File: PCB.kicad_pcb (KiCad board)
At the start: 2 copper layers, 60 x 60 mm, 50 parts, among them J1 USB_C_Receptacle_USB2.0_16P, J2 Conn_01x04_Pin, J3 Conn_01x04_Pin, J4 Conn_01x04_Pin, J5 Conn_01x02_Pin, J6 Conn_01x02_Pin, J7 Conn_01x02_Pin, SW1 SW_Push, SW2 SW_Push, U1 TMC2209_SILENTSTEPSTICK, U2 TMC2209_SILENTSTEPSTICK, U3 D3V3XA4B10LP, U4 AMS1117-3.3 (UMW), U5 TMC2209_SILENTSTEPSTICK, U6 ESP32-S3-WROOM-1

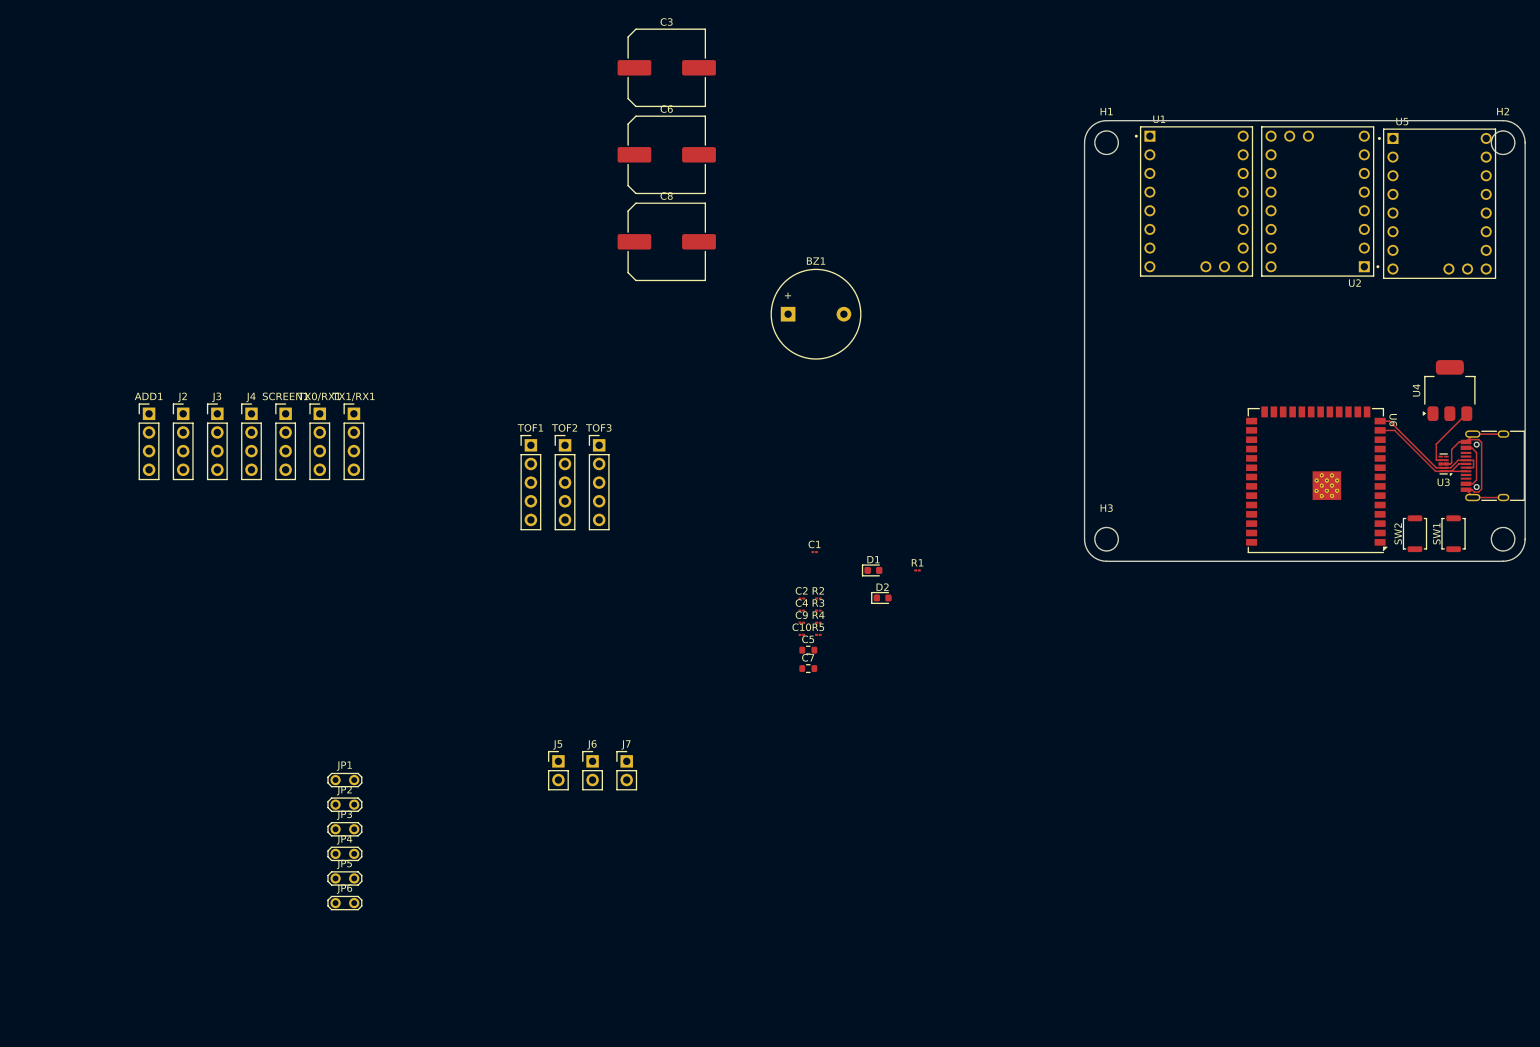
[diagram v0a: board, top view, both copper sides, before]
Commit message: Correction bug schématic
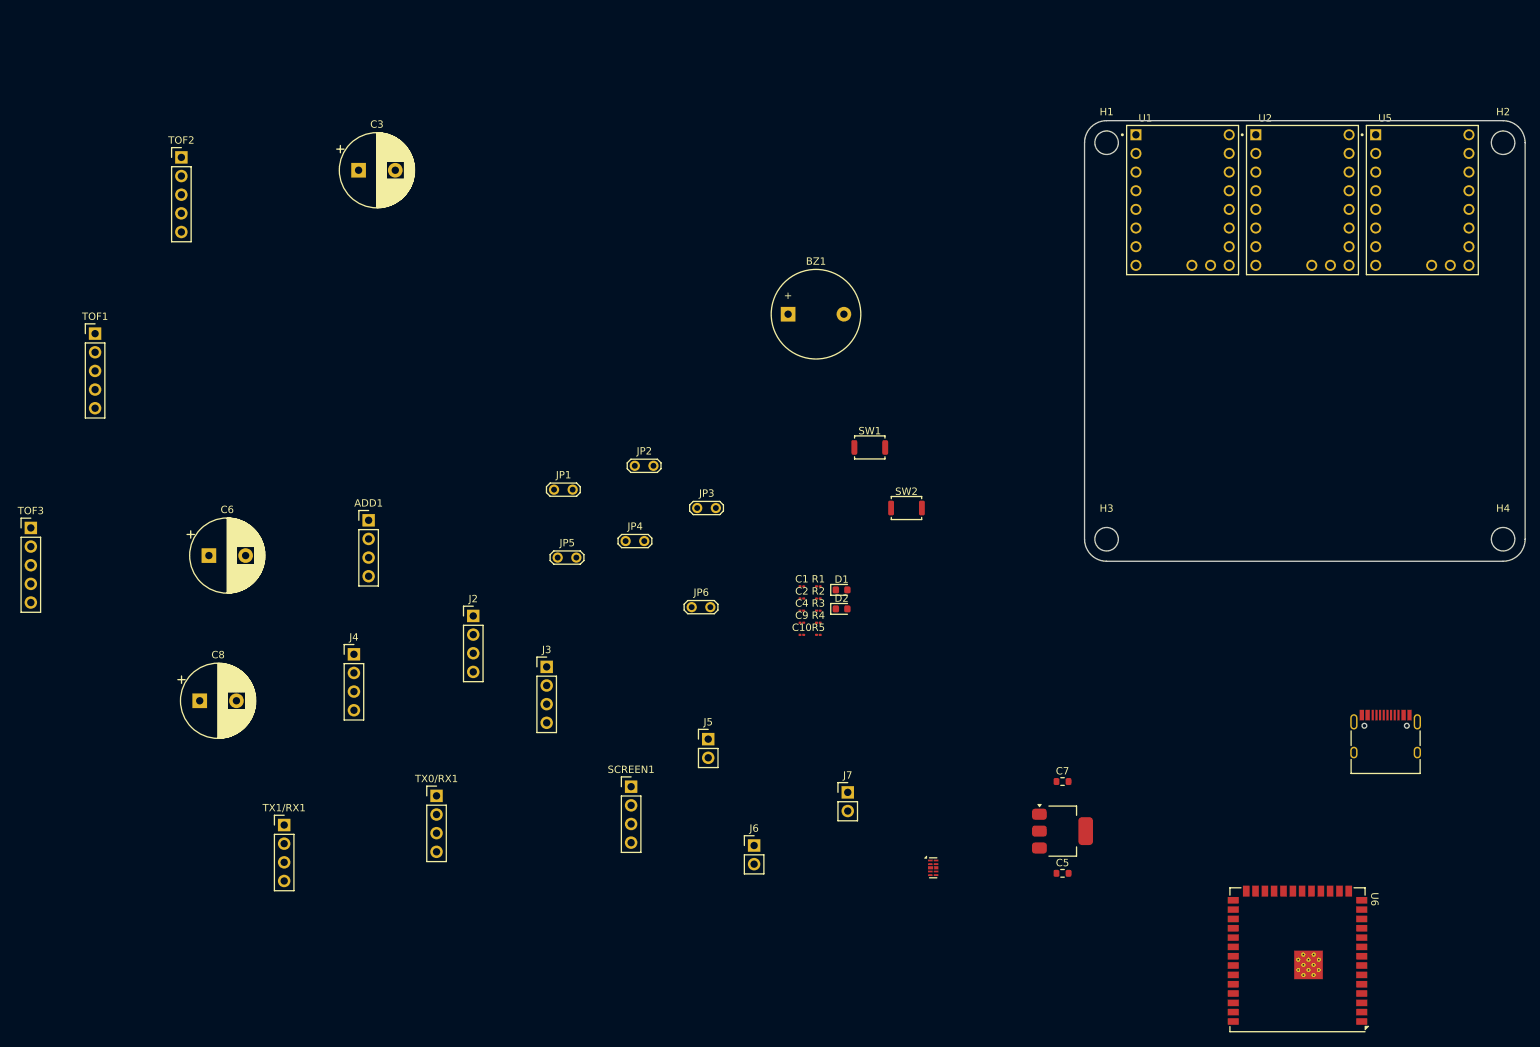
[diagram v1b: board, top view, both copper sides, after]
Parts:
- C3, C6, C8: footprint Capacitor_SMD:C_Elec_10x10.2 -> Capacitor_THT:CP_Radial_D10.0mm_P5.00mm
- moved C8 89.2 mm to (89.5, 126.0)
- moved U3 88.6 mm to (189.4, 148.8), turned to 0 degrees
- moved C6 82.9 mm to (90.8, 106.2)
- moved SW1 80.4 mm to (180.8, 91.5), turned to 0 degrees
- moved U4 79.9 mm to (207.0, 143.8), turned to 0 degrees
- moved TOF3 78.2 mm to (66.5, 102.5)
- moved SW2 69.3 mm to (185.8, 99.8), turned to 0 degrees
- moved SCREEN1 69.2 mm to (148.2, 137.7)
- moved JP3 65.9 mm to (157.2, 99.8)
- moved TOF2 65.3 mm to (87.0, 52.0)
- moved U6 65.3 mm to (239.0, 161.3)
- moved JP6 63.1 mm to (156.5, 113.2)
- moved JP2 61.6 mm to (148.8, 94.0)
- moved TOF1 61.3 mm to (75.2, 76.0)
- moved JP4 58.1 mm to (147.5, 104.2)
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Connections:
- ADD1 pad 4: 3V3 -> GND
- BZ1 pad 2: 3V3 -> GND
- C1 pad 2: 3V3 -> GND
- C10 pad 2: 3V3 -> GND
- C2 pad 2: 3V3 -> GND
- C3 pad 2: 3V3 -> GND
- C4 pad 2: 3V3 -> GND
- C5 pad 2: 3V3 -> GND
- C6 pad 2: 3V3 -> GND
- C7 pad 2: 3V3 -> GND
- C8 pad 2: 3V3 -> GND
- C9 pad 2: 3V3 -> GND
- J1 pad A1: 3V3 -> GND
- J1 pad A12: 3V3 -> GND
- J1 pad B1: 3V3 -> GND
- J1 pad B12: 3V3 -> GND
- J1 pad S1: 3V3 -> GND
- J5 pad 2: 3V3 -> GND
- J7 pad 2: 3V3 -> GND
- R2 pad 2: 3V3 -> GND
- R3 pad 2: 3V3 -> GND
- R4 pad 2: 3V3 -> GND
- R5 pad 2: 3V3 -> GND
- SCREEN1 pad 4: 3V3 -> GND
- SW1 pad 1: 3V3 -> GND
- SW2 pad 1: 3V3 -> GND
- TOF1 pad 4: 3V3 -> GND
- TOF2 pad 4: 3V3 -> GND
- TOF3 pad 4: 3V3 -> GND
- TX0/RX1 pad 1: 3V3 -> GND
- TX1/RX1 pad 1: 3V3 -> GND
- U1 pad 1: 3V3 -> GND
- U1 pad 16: 3V3 -> GND
- U1 pad 7: 3V3 -> GND
- U2 pad 1: 3V3 -> GND
- U2 pad 16: 3V3 -> GND
- U2 pad 7: 3V3 -> GND
- U3 pad 3: 3V3 -> GND
- U3 pad 8: 3V3 -> GND
- U4 pad 1: 3V3 -> GND
- U5 pad 1: 3V3 -> GND
- U5 pad 16: 3V3 -> GND
- U5 pad 7: 3V3 -> GND
- U6 pad 1: 3V3 -> GND
- U6 pad 40: 3V3 -> GND
- U6 pad 41: 3V3 -> GND
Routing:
- net 3V3: track 29.5 -> 0.00 mm
- net USB_N: track 18.6 -> 0.00 mm
- net USB_P: track 18.5 -> 0.00 mm
- net VCC_5V: track 9.40 -> 0.00 mm
- net VCC_5Vin: track 7.08 -> 0.00 mm

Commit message: routage terminé
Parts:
- removed J4: Conn_01x04_Pin, Connector_PinHeader_2.54mm:PinHeader_1x04_P2.54mm_Vertical
- added J8: Conn_01x04_Pin, Connector_PinHeader_2.54mm:PinHeader_1x04_P2.54mm_Vertical, F.Cu at (125.6, 98.2)
- moved U6 106.6 mm to (139.5, 122.9)
- moved H1 103.1 mm to (113.2, 76.0)
- moved H3 103.1 mm to (113.2, 130.0)
- moved H2 103.1 mm to (167.2, 76.0)
- moved H4 103.1 mm to (167.2, 130.0)
- moved U1 102.8 mm to (123.9, 83.8)
- moved U2 102.8 mm to (140.2, 83.8)
- moved U5 102.8 mm to (156.5, 83.8)
- moved J1 86.0 mm to (166.0, 118.6), turned to 90 degrees
- moved C8 80.8 mm to (154.1, 77.4)
- moved SW1 66.5 mm to (126.5, 130.0), turned to 90 degrees
- moved TOF2 61.3 mm to (121.2, 102.9)
- moved TOF3 57.3 mm to (123.8, 102.9)
- moved C5 56.9 mm to (165.2, 110.9), turned to 180 degrees
- moved U4 56.1 mm to (165.2, 106.3)
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- renumbered ADD1 to ADD, SCREEN1 to SCREEN
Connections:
- J2 pad 1: Net-(J2-Pin_1) -> MOTORB1
- J2 pad 2: Net-(J2-Pin_2) -> MOTORB2
- J2 pad 3: Net-(J2-Pin_3) -> MOTORB3
- J2 pad 4: Net-(J2-Pin_4) -> MOTORB4
- J3 pad 1: Net-(J3-Pin_1) -> MOTORC1
- J3 pad 2: Net-(J3-Pin_2) -> MOTORC2
- J3 pad 3: Net-(J3-Pin_3) -> MOTORC3
- J3 pad 4: Net-(J3-Pin_4) -> MOTORC4
- U1 pad 3: Net-(J2-Pin_2) -> MOTORA1
- U1 pad 4: Net-(J2-Pin_4) -> MOTORA2
- U1 pad 5: Net-(J2-Pin_3) -> MOTORA3
- U1 pad 6: Net-(J2-Pin_1) -> MOTORA4
- U2 pad 3: Net-(J3-Pin_2) -> MOTORB1
- U2 pad 4: Net-(J3-Pin_4) -> MOTORB2
- U2 pad 5: Net-(J3-Pin_3) -> MOTORB3
- U2 pad 6: Net-(J3-Pin_1) -> MOTORB4
- U5 pad 3: Net-(J4-Pin_2) -> MOTORC1
- U5 pad 4: Net-(J4-Pin_4) -> MOTORC2
- U5 pad 5: Net-(J4-Pin_3) -> MOTORC3
- U5 pad 6: Net-(J4-Pin_1) -> MOTORC4
- U6 pad 19: STEP1 -> STEP3
- U6 pad 21: STEP3 -> STEP1
- U6 pad 4: BUZZER -> LED
- U6 pad 5: LED -> BUZZER
- U6 pad 8: DIR2 -> DIR3
- U6 pad 9: DIR3 -> DIR2
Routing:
- net GND: track 0.00 -> 423.9 mm
- net VCC_5V: track 0.00 -> 276.3 mm, vias 0 -> 4
- net 3V3: track 0.00 -> 59.7 mm
- net STEP3: track 0.00 -> 58.7 mm, vias 0 -> 1
- net DIR3: track 0.00 -> 55.8 mm
- net DIR1: track 0.00 -> 42.8 mm
- net SDA: track 0.00 -> 42.3 mm, vias 0 -> 1
- net STEP2: track 0.00 -> 40.5 mm
- net STEP1: track 0.00 -> 39.7 mm
- net XSHUT1: track 0.00 -> 39.4 mm, vias 0 -> 2
- net XSHUT2: track 0.00 -> 35.5 mm, vias 0 -> 2
- net SCL: track 0.00 -> 32.9 mm
- net USB_P: track 0.00 -> 32.8 mm, vias 0 -> 2
- net TX1: track 0.00 -> 32.8 mm, vias 0 -> 1
- net RX1: track 0.00 -> 32.6 mm, vias 0 -> 1
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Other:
- board text added: "DRIVER1"
- board text added: "DRIVER2"
- board text added: "DRIVER3"

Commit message: chnagement jumper + orga
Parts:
- added J4: Conn_01x07_Pin, Connector_PinHeader_2.54mm:PinHeader_1x04_P2.54mm_Vertical, F.Cu at (137.2, 105.4)
- added J9: Conn_01x07_Pin, Connector_PinHeader_2.54mm:PinHeader_1x03_P2.54mm_Vertical, F.Cu at (137.2, 108.0)
- JP1, JP2, JP3, JP4, JP5, JP6: footprint TestPoint:TestPoint_2Pads_Pitch2.54mm_Drill0.8mm -> Connector_PinHeader_2.54mm:PinHeader_1x02_P2.54mm_Vertical
- moved ADD1 15.6 mm to (127.0, 116.8), turned to -90 degrees
- moved SCREEN1 8.87 mm to (127.0, 114.3), turned to -90 degrees
- moved TOF1 8.42 mm to (127.0, 104.1), turned to -90 degrees
- moved TOF3 7.10 mm to (127.0, 109.2), turned to -90 degrees
- moved TOF2 6.91 mm to (127.0, 106.7), turned to -90 degrees
- moved UART1 5.05 mm to (124.6, 121.3), turned to -90 degrees
- moved C6 2.55 mm to (137.7, 75.0)
- moved C3 2.53 mm to (121.4, 75.0)
- moved C8 2.53 mm to (154.0, 74.9)
- moved UART0 2.24 mm to (124.6, 123.8), turned to -90 degrees
- moved R5 1.13 mm to (157.0, 123.2)
- moved JP4 1.06 mm to (138.7, 89.5), turned to 90 degrees
- moved JP3 0.92 mm to (138.7, 92.0), turned to 90 degrees
- moved JP2 0.37 mm to (123.2, 90.0), turned to 90 degrees
- moved JP6 0.28 mm to (155.7, 90.0), turned to 90 degrees
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- renumbered ADD to ADD1, SCREEN to SCREEN1, TX0/RX1 to UART0, TX1/RX1 to UART1
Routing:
- net GND: track 423.9 -> 561.0 mm, vias 0 -> 1
- net DIR2: track 0.00 -> 49.8 mm
- net GPIO38: track 0.00 -> 28.2 mm, vias 0 -> 1
- net GPIO47: track 0.00 -> 27.8 mm, vias 0 -> 1
- net GPIO37: track 0.00 -> 23.7 mm, vias 0 -> 1
- net GPIO35: track 0.00 -> 23.7 mm, vias 0 -> 1
- net GPIO48: track 0.00 -> 12.6 mm, vias 0 -> 1
- net VCC_5V: track 276.3 -> 266.3 mm
- net XSHUT2: track 35.5 -> 26.1 mm
- net XSHUT3: track 31.2 -> 23.1 mm
- net XSHUT1: track 39.4 -> 31.8 mm
- net SDA: track 42.3 -> 35.2 mm, vias 1 -> 2
- net GPIO21: track 0.00 -> 6.39 mm, vias 0 -> 1
- net Net-(JP6-B): track 0.00 -> 5.57 mm
- net Net-(JP5-B): track 0.00 -> 5.57 mm
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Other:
- board text added: "5V"
- board text added: "BOOT"
- board text added: "GND"
- board text added: "GPIOs"
- board text added: "RST"
- board text added: "RX"
- board text added: "SCL"
- board text added: "SDA"
- board text added: "TX"
- board text added: "X"

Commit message: ajout plus de 5V et GND
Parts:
- added J10: Conn_01x05_Pin, Connector_PinHeader_2.54mm:PinHeader_1x05_P2.54mm_Vertical, F.Cu at (167.4, 81.4)
- added J11: Conn_01x05_Pin, Connector_PinHeader_2.54mm:PinHeader_1x05_P2.54mm_Vertical, F.Cu at (113.0, 81.3)
- added JP7: Jumper_2_Open, Resistor_SMD:R_1206_3216Metric_Pad1.30x1.75mm_HandSolder, F.Cu at (113.2, 98.2)
- added JP8: Jumper_2_Open, Resistor_SMD:R_1206_3216Metric_Pad1.30x1.75mm_HandSolder, F.Cu at (113.2, 95.5)
- renumbered ADD1 to ADD, SCREEN1 to SCREEN
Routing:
- net VCC_5V: track 266.3 -> 323.2 mm
- net GND: track 561.0 -> 584.4 mm
- net GPIO36: track 0.00 -> 19.9 mm, vias 0 -> 2
- net SDA: track 35.2 -> 53.4 mm, vias 2 -> 3
- net SCL: track 31.4 -> 48.7 mm, vias 0 -> 2
- net XSHUT3: track 23.1 -> 23.7 mm
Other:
- board text added: "21"
- board text added: "35"
- board text added: "36"
- board text added: "37"
- board text added: "38"
- board text added: "47"
- board text added: "48"
- board text added: "Amiens"
- board text added: "Unimakers"

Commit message: Test DRC + corrections
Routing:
- net GPIO0: track 19.4 -> 23.9 mm
- net GND: track 584.4 -> 583.1 mm
- net DIR3: track 55.8 -> 56.7 mm
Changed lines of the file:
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@@
 	)
 	(segment
+		(start 129.16 119)
+		(end 127 116.84)
+		(width 0.2)
+		(layer "F.Cu")
+		(net 1)
+	)
+	(segment
 		(start 113.85 96.45)
 		(end 113.85 101.6)
@@
 	)
 	(segment
-		(start 128.76 118.6)
-		(end 127 116.84)
-		(width 0.2)
-		(layer "F.Cu")
-		(net 1)
-	)
-	(segment
 		(start 133.2 119.2)
 		(end 135.46 121.46)
@@
 	)
 	(segment
-		(start 128.8 118.6)
-		(end 128.76 118.6)
+		(start 114.8 95.5)
+		(end 113.85 96.45)
 		(width 0.2)
 		(layer "F.Cu")
@@
 	)
 	(segment
-		(start 114.8 95.5)
-		(end 113.85 96.45)
+		(start 129.2 119)
+		(end 129.16 119)
 		(width 0.2)
 		(layer "F.Cu")
@@
 	)
 	(via
-		(at 128.8 118.6)
+		(at 129.2 119)
 		(size 0.6)
 		(drill 0.3)
@@
 	)
 	(segment
-		(start 133.2 119.2)
-		(end 129.4 119.2)
-		(width 0.2)
-		(layer "B.Cu")
-		(net 1)
-	)
-	(segment
 		(start 122.07 101.75)
 		(end 124.46 104.14)
@@
 	(segment
 		(start 129.4 119.2)
-		(end 128.8 118.6)
+		(end 133.2 119.2)
 		(width 0.2)
 		(layer "B.Cu")
@@
 	)
 	(segment
+		(start 129.2 119)
+		(end 129.4 119.2)
+		(width 0.2)
+		(layer "B.Cu")
+		(net 1)
+	)
+	(segment
 		(start 129.81 128.76)
 		(end 130.76 128.76)
@@
 	)
 	(segment
+		(start 121.35 73.6)
+		(end 132.43 73.6)
+		(width 0.2)
+		(layer "F.Cu")
+		(net 4)
+	)
+	(segment
 		(start 158.01 94.98)
 		(end 158.21 94.98)
@@
 	)
 	(segment
+		(start 132.79 73.6)
+		(end 146.752 73.6)
+		(width 0.2)
+		(layer "F.Cu")
+		(net 4)
+	)
+	(segment
 		(start 123.225 92.5)
 		(end 123.225 89.96)
@@
 	)
 	(segment
-		(start 146.932 73.78)
-		(end 150.16 77.008)
-		(width 0.2)
-		(layer "F.Cu")
-		(net 4)
-	)
-	(segment
 		(start 165.623 112.467)
 		(end 165.623 111.242)
@@
 	)
 	(segment
-		(start 116.456 78.494)
-		(end 117.51 77.44)
+		(start 132.61 73.78)
+		(end 132.79 73.6)
 		(width 0.2)
 		(layer "F.Cu")
@@
 	)
 	(segment
-		(start 117.51 78.26)
+		(start 116.456 78.494)
 		(end 117.51 77.44)
 		(width 0.2)
@@
 	)
 	(segment
-		(start 121.17 73.78)
-		(end 132.61 73.78)
+		(start 117.51 78.26)
+		(end 117.51 77.44)
 		(width 0.2)
 		(layer "F.Cu")
@@
 	)
 	(segment
-		(start 149.106 91.626)
-		(end 149.106 78.494)
+		(start 150.16 77.008)
+		(end 150.16 77.44)
 		(width 0.2)
 		(layer "F.Cu")
@@
 	)
 	(segment
-		(start 132.61 73.78)
-		(end 146.932 73.78)
+		(start 149.106 91.626)
+		(end 149.106 78.494)
 		(width 0.2)
 		(layer "F.Cu")
@@
 	)
 	(segment
+		(start 132.43 73.6)
+		(end 132.61 73.78)
+		(width 0.2)
+		(layer "F.Cu")
+		(net 4)
+	)
+	(segment
 		(start 132.61 73.78)
 		(end 132.61 76.215)
@@
 	)
 	(segment
-		(start 117.51 77.44)
-		(end 121.17 73.78)
+		(start 146.752 73.6)
+		(end 150.16 77.008)
 		(width 0.2)
 		(layer "F.Cu")
@@
 	)
 	(segment
-		(start 150.16 77.008)
-		(end 150.16 77.44)
+		(start 117.51 77.44)
+		(end 121.35 73.6)
 		(width 0.2)
 		(layer "F.Cu")
@@
 	)
 	(segment
-		(start 128.71 114.98)
-		(end 128.9 114.79)
+		(start 130.76 113.86)
+		(end 130.76 114.79)
 		(width 0.2)
 		(layer "F.Cu")
@@
 	)
 	(segment
-		(start 128.9 114.79)
-		(end 130.76 114.79)
+		(start 128.9 112)
+		(end 130.76 113.86)
 		(width 0.2)
 		(layer "F.Cu")
@@
 	)
 	(via
-		(at 128.71 114.98)
+		(at 128.9 112)
 		(size 0.6)
 		(drill 0.3)
@@
 	)
 	(segment
-		(start 127.21 116.48)
-		(end 128.71 114.98)
+		(start 128.4 119.79)
+		(end 127.21 120.98)
+		(width 0.2)
+		(layer "B.Cu")
+		(net 6)
+	)
+	(segment
+		(start 128.4 112.5)
+		(end 128.4 119.79)
 		(width 0.2)
 		(layer "B.Cu")
@@
 	)
 	(segment
-		(start 127.21 120.98)
-		(end 127.21 116.48)
+		(start 128.9 112)
+		(end 128.4 112.5)
 		(width 0.2)
 		(layer "B.Cu")
@@
 	)
 	(segment
+		(start 156.15 123.25)
+		(end 156.725 123.25)
+		(width 0.2)
+		(layer "F.Cu")
+		(net 10)
+	)
+	(segment
 		(start 155.91 125.4925)
-		(end 155.91 124.065)
+		(end 155.91 123.49)
 		(width 0.2)
 		(layer "F.Cu")
@@
 	)
 	(segment
-		(start 155.91 124.065)
-		(end 156.725 123.25)
+		(start 155.91 123.49)
+		(end 156.15 123.25)
 		(width 0.2)
 		(layer "F.Cu")
@@
 	)
 	(segment
-		(start 143.125 90.14)
-		(end 146.535 90.14)
+		(start 146.535 90.14)
+		(end 143.125 90.14)
 		(width 0.2)
 		(layer "F.Cu")
@@
 	)
 	(segment
-		(start 141.265 92)
-		(end 143.125 90.14)
+		(start 143.125 90.14)
+		(end 141.265 92)
 		(width 0.2)
 		(layer "F.Cu")
@@
 	(segment
 		(start 143.125 87.6)
-		(end 146.535 87.6)
+		(end 141.265 89.46)
 		(width 0.2)
 		(layer "F.Cu")
@@
 	)
 	(segment
-		(start 141.265 89.46)
+		(start 146.535 87.6)
 		(end 143.125 87.6)
 		(width 0.2)
@@
 	)
 	(segment
-		(start 146.4 98.2)
-		(end 146.4 110.14)
+		(start 146.4 110.14)
+		(end 144.05 112.49)
 		(width 0.2)
 		(layer "F.Cu")
@@
 	)
 	(segment
-		(start 140 83.975)
-		(end 140 91.8)
+		(start 146.535 77.44)
+		(end 140 83.975)
 		(width 0.2)
 		(layer "F.Cu")
@@
 	)
 	(segment
-		(start 146.4 110.14)
-		(end 144.05 112.49)
+		(start 140.665 112.49)
+		(end 140.145 113.01)
 		(width 0.2)
 		(layer "F.Cu")
@@
 	)
 	(segment
-		(start 146.535 77.44)
-		(end 140 83.975)
+		(start 140 92.8)
+		(end 146.4 99.2)
 		(width 0.2)
 		(layer "F.Cu")
@@
 	)
 	(segment
-		(start 144.05 112.49)
-		(end 140.665 112.49)
+		(start 140 83.975)
+		(end 140 92.8)
 		(width 0.2)
 		(layer "F.Cu")
@@
 	)
 	(segment
-		(start 140.665 112.49)
-		(end 140.145 113.01)
+		(start 144.05 112.49)
+		(end 140.665 112.49)
 		(width 0.2)
 		(layer "F.Cu")
@@
 	)
 	(segment
-		(start 140 91.8)
-		(end 146.4 98.2)
+		(start 146.4 99.2)
+		(end 146.4 110.14)
 		(width 0.2)
 		(layer "F.Cu")
@@
 	)
 	(segment
-		(start 159.23 99.13)
-		(end 159.23 79.38)
+		(start 159.23 96.57)
+		(end 160.8 95)
 		(width 0.2)
 		(layer "F.Cu")
@@
 	)
 	(segment
-		(start 159.23 79.38)
-		(end 162.86 75.75)
+		(start 159.23 99.13)
+		(end 159.23 96.57)
 		(width 0.2)
 		(layer "F.Cu")
@@
 	)
 	(segment
+		(start 160.8 76.96)
+		(end 162.86 74.9)
+		(width 0.2)
+		(layer "F.Cu")
+		(net 46)
+	)
+	(segment
+		(start 160.8 95)
+		(end 160.8 76.96)
+		(width 0.2)
+		(layer "F.Cu")
+		(net 46)
+	)
+	(segment
 		(start 148.79 122.41)
 		(end 151.79 119.41)
@@
 	)
 	(segment
+		(start 158 121.54)
+		(end 159.26 120.28)
+		(width 0.2)
+		(layer "F.Cu")
+		(net 64)
+	)
+	(segment
 		(start 130.21 95.9)
 		(end 130.21 92.68)
@@
 	)
 	(segment
+		(start 157.95 123.25)
+		(end 158 123.2)
+		(width 0.2)
+		(layer "F.Cu")
+		(net 64)
+	)
+	(segment
 		(start 119.38 109.22)
 		(end 119.38 104.14)
@@
 	)
 	(segment
+		(start 158 123.2)
+		(end 158 121.54)
+		(width 0.2)
+		(layer "F.Cu")
+		(net 64)
+	)
+	(segment
 		(start 163.689594 115.015)
 		(end 162.28 115.015)
@@
 	)
 	(segment
-		(start 157.225 122.315)
-		(end 159.26 120.28)
-		(width 0.2)
-		(layer "F.Cu")
-		(net 64)
-	)
-	(segment
 		(start 162.88 114.26)
 		(end 167.06 114.26)
@@
 	)
 	(segment
-		(start 159.26 122.08)
-		(end 159.26 120.28)
-		(width 0.2)
-		(layer "F.Cu")
-		(net 64)
-	)
-	(segment
 		(start 147.605736 131.3)
 		(end 148.26 131.3)
@@
 	)
 	(segment
-		(start 157.225 123.25)
-		(end 157.225 122.315)
-		(width 0.2)
-		(layer "F.Cu")
-		(net 64)
-	)
-	(segment
 		(start 129.51 130.14841)
 		(end 127.57841 132.08)
@@
 		(width 0.2)
 		(layer "F.Cu")
+		(net 64)
+	)
+	(segment
+		(start 157.225 123.25)
+		(end 157.95 123.25)
+		(width 0.2)
+		(layer "F.Cu")
